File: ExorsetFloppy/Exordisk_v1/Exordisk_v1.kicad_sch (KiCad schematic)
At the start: 28 parts, among them J1 BUS, J4 Conn_01x01, J5 Conn_01x01, J6 Conn_01x01, U1 GAL22V10, U11 74HCT74, U12 74HCT74, U15 74HCT04, U16 74HCT74, U17 74HCT00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

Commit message: 74LS73 ch. to LS112
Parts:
- removed U19: 74LS73, Package_DIP:DIP-14_W7.62mm, symbol 74xx:74LS73
- added U19: 74LS112, Package_DIP:DIP-16_W7.62mm, symbol 74xx:74LS112
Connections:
- net +5V: now also U19.15 (~{R}), U19.16 (VCC), U19.2 (K), U19.3 (J), U19.4 (~{S})
- net Floppy Logic/CLK500k: now also U19.5 (Q)
- net GND: now also U19.8 (GND)
- net at JP8.2 (C): now also U19.1 (C)
- no-connect marks 7 -> 8

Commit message: build script new
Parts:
- removed U6: 27C32, Package_DIP:DIP-24_W15.24mm, symbol my_ics_new:27C32
- added JP9: SolderJumper_2_Open, Jumper:SolderJumper-2_P1.3mm_Open_Pad1.0x1.5mm, symbol Jumper:SolderJumper_2_Open
- added U14: 27C64, Package_DIP:DIP-28_W15.24mm, symbol Memory_EPROM:27C64
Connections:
- net +5V: now also U14.27 (~{PGM}), U14.28 (VCC)
- net BA0: now also U14.10 (A0)
- net BA1: now also U14.9 (A1)
- net BA10: now also U14.21 (A10)
- net BA11: now also U14.23 (A11)
- net BA12: now also U14.2 (A12)
- net BA2: now also U14.8 (A2)
- net BA3: now also U14.7 (A3)
- net BA4: now also U14.6 (A4)
- net BA5: now also U14.5 (A5)
- net BA6: now also U14.4 (A6)
- net BA7: now also U14.3 (A7)
- net BA8: now also U14.25 (A8)
- net BA9: now also U14.24 (A9)
- net D0: now also U14.11 (D0)
- net D1: now also U14.12 (D1)
- net D2: now also U14.13 (D2)
- net D3: now also U14.15 (D3)
- net D4: now also U14.16 (D4)
- net D5: now also U14.17 (D5)
- net D6: now also U14.18 (D6)
- net D7: now also U14.19 (D7)
- net GND: now also JP9.1 (A), U14.14 (GND), U14.20 (~{CE})
- net ~{ROM_CS}: now also U14.22 (~{OE})
- new net: JP9.2 (B), U14.1 (VPP)
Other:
- note added: "(E800-EBFF) Standard place ED00-EFFF"
- note added: "BA10 and BA11 and are always high when EPROM is selected, BA12 is low."
- note added: "Mapped to ED00-EFFF. EPROM starts @ E000 but E000-ECFF is not useable. In EPROM Adresses: start @ D00-FFF."
- note removed: "E800-EBFF"

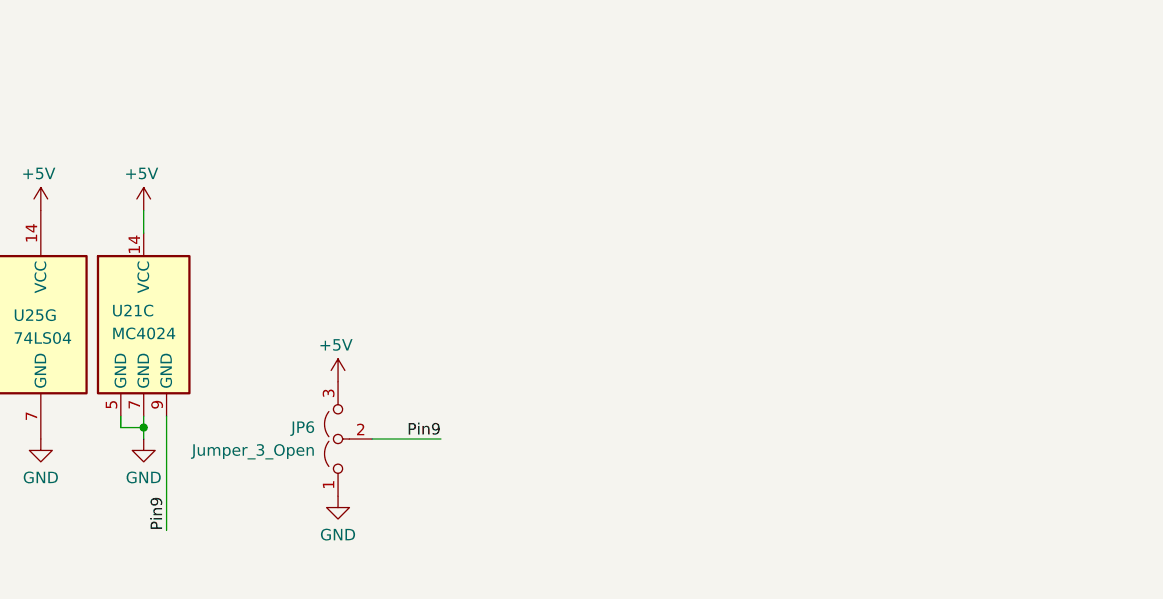
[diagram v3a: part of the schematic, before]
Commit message: new build for extra drives
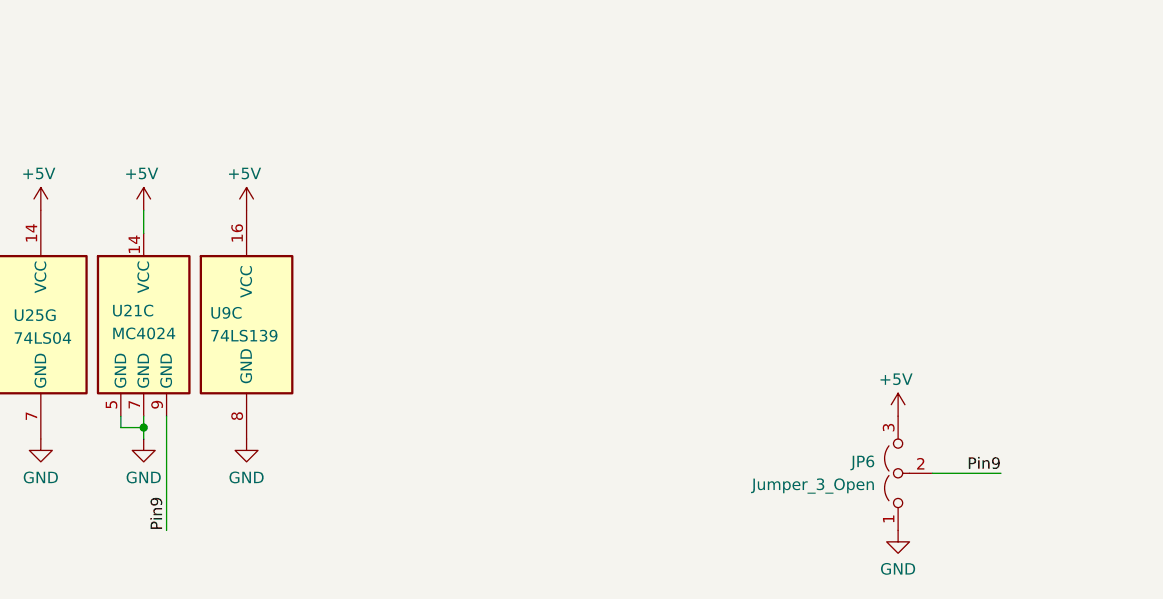
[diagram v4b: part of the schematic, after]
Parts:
- added U9: 74LS139, Package_DIP:DIP-16_W7.62mm, symbol 74xx:74LS139
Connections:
- net +5V: now also U9.16 (VCC)
- net GND: now also U9.8 (GND)
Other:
- moved on the sheet: JP6

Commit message: Exordisk Board continued
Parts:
- added U9: 74LS32, Package_DIP:DIP-14_W7.62mm, symbol 74xx:74LS32
- renumbered U9 to U6
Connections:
- net +5V: now also U9.14 (VCC)
- net GND: now also U9.7 (GND)
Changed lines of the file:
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@@
+	(symbol
+		(lib_id "power:GND")
+		(at 165.1 265.43 0)
+		(unit 1)
+		(exclude_from_sim no)
+		(in_bom yes)
+		(on_board yes)
+		(dnp no)
+		(property "Reference" "#PWR0132"
+			(at 165.1 271.78 0)
+			(effects
+				(font
+					(size 1.27 1.27)
+				)
+				(hide yes)
+			)
+		)
+		(property "Value" "GND"
+			(at 165.1 269.748 0)
+			(effects
+				(font
+					(size 1.27 1.27)
+				)
+			)
+		)
+		(property "Footprint" ""
+			(at 165.1 265.43 0)
+			(effects
+				(font
+					(size 1.27 1.27)
+				)
+				(hide yes)
+			)
+		)
+		(property "Datasheet" ""
+			(at 165.1 265.43 0)
+			(effects
+				(font
+					(size 1.27 1.27)
+				)
+				(hide yes)
+			)
+		)
+		(property "Description" "Power symbol creates a global label with name \"GND\" , ground"
+			(at 165.1 265.43 0)
+			(effects
+				(font
+					(size 1.27 1.27)
+				)
+				(hide yes)
+			)
+		)
+		(pin "1"
+		)
+		(instances
+			(project "Exordisk_v1"
+				(path "/05fb24d5-db99-47c3-b50e-9b588fa507ac"
+					(reference "#PWR0132")
+					(unit 1)
+				)
+			)
+		)
+	)
 	(symbol
 		(lib_id "power:GND")
@@
 	)
 	(symbol
+		(lib_id "power:+5V")
+		(at 165.1 240.03 0)
+		(unit 1)
+		(exclude_from_sim no)
+		(in_bom yes)
+		(on_board yes)
+		(dnp no)
+		(property "Reference" "#PWR0131"
+			(at 165.1 243.84 0)
+			(effects
+				(font
+					(size 1.27 1.27)
+				)
+				(hide yes)
+			)
+		)
+		(property "Value" "+5V"
+			(at 164.846 235.966 0)
+			(effects
+				(font
+					(size 1.27 1.27)
+				)
+			)
+		)
+		(property "Footprint" ""
+			(at 165.1 240.03 0)
+			(effects
+				(font
+					(size 1.27 1.27)
+				)
+				(hide yes)
+			)
+		)
+		(property "Datasheet" ""
+			(at 165.1 240.03 0)
+			(effects
+				(font
+					(size 1.27 1.27)
+				)
+				(hide yes)
+			)
+		)
+		(property "Description" "Power symbol creates a global label with name \"+5V\""
+			(at 165.1 240.03 0)
+			(effects
+				(font
+					(size 1.27 1.27)
+				)
+				(hide yes)
+			)
+		)
+		(pin "1"
+		)
+		(instances
+			(project "Exordisk_v1"
+				(path "/05fb24d5-db99-47c3-b50e-9b588fa507ac"
+					(reference "#PWR0131")
+					(unit 1)
+				)
+			)
+		)
+	)
+	(symbol
 		(lib_id "74xx:74LS04")
 		(at 130.81 252.73 0)
@@
 		(on_board yes)
 		(dnp no)
-		(property "Reference" "U9"
+		(property "Reference" "U6"
 			(at 149.606 251.46 0)
 			(effects
@@
 			(project "Exordisk_v1"
 				(path "/05fb24d5-db99-47c3-b50e-9b588fa507ac"
-					(reference "U9")
+					(reference "U6")
 					(unit 3)
 				)
@@
 				)
 			)
+		)
+	)
+	(symbol
+		(lib_id "74xx:74LS32")
+		(at 165.1 252.73 0)
+		(unit 5)
+		(exclude_from_sim no)
+		(in_bom yes)
+		(on_board yes)
+		(dnp no)
+		(property "Reference" "U9"
+			(at 161.29 251.206 0)
+			(effects
+				(font
+					(size 1.27 1.27)
+				)
+				(justify left)
+			)
+		)
+		(property "Value" "74LS32"
+			(at 161.29 253.746 0)
+			(effects
+				(font
+					(size 1.27 1.27)
+				)
+				(justify left)
+			)
+		)
+		(property "Footprint" "Package_DIP:DIP-14_W7.62mm"
+			(at 165.1 252.73 0)
+			(effects
+				(font
+					(size 1.27 1.27)
+				)
+				(hide yes)
+			)
+		)
+		(property "Datasheet" "http://www.ti.com/lit/gpn/sn74LS32"
+			(at 165.1 252.73 0)
+			(effects
+				(font
+					(size 1.27 1.27)
+				)
+				(hide yes)
+			)
+		)
+		(property "Description" "Quad 2-input OR"
+			(at 165.1 252.73 0)
+			(effects
+				(font
+					(size 1.27 1.27)
+				)
+				(hide yes)
+			)
+		)
+		(pin "6"
+		)
+		(pin "2"
+		)
+		(pin "12"
+		)
+		(pin "10"
+		)
+		(pin "13"
+		)
+		(pin "3"
+		)
+		(pin "7"
+		)
+		(pin "11"
+		)
+		(pin "8"
+		)
+		(pin "9"
+		)
+		(pin "1"
+		)
+		(pin "4"
+		)
+		(pin "5"
+		)
+		(pin "14"
+		)
+		(instances
+			(project ""
+				(path "/05fb24d5-db99-47c3-b50e-9b588fa507ac"
+					(reference "U9")
+					(unit 5)
+				)
+			)
